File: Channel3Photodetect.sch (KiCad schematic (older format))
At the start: 5 parts

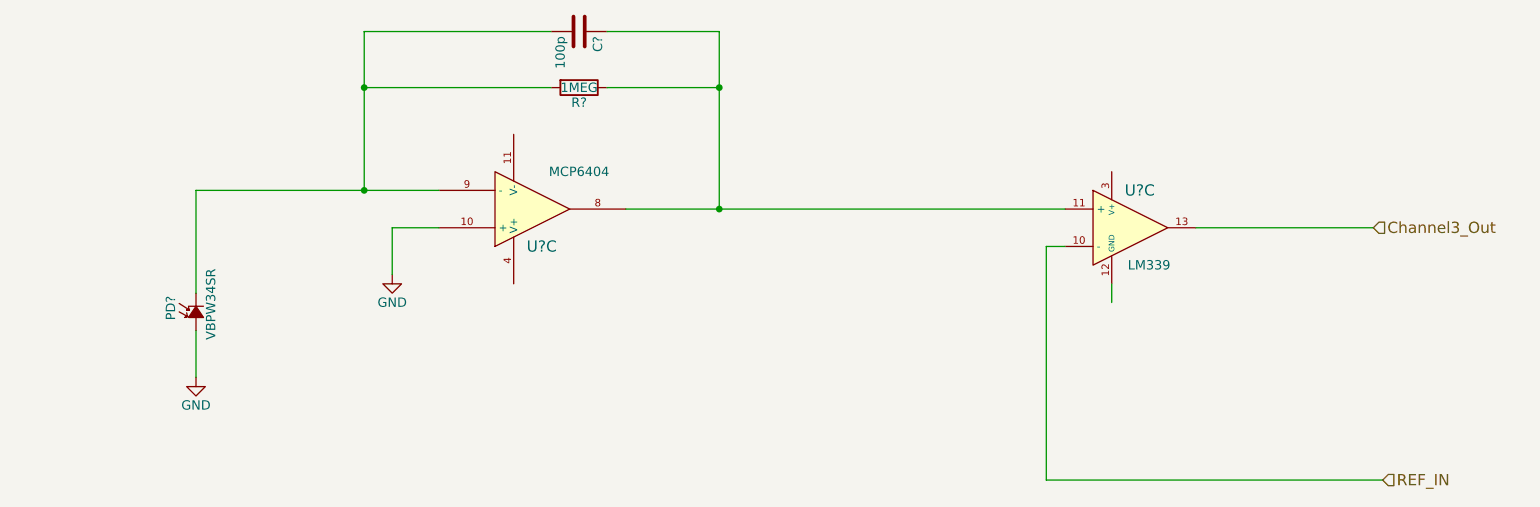
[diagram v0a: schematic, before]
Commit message: Added power regulator, VGND and test points
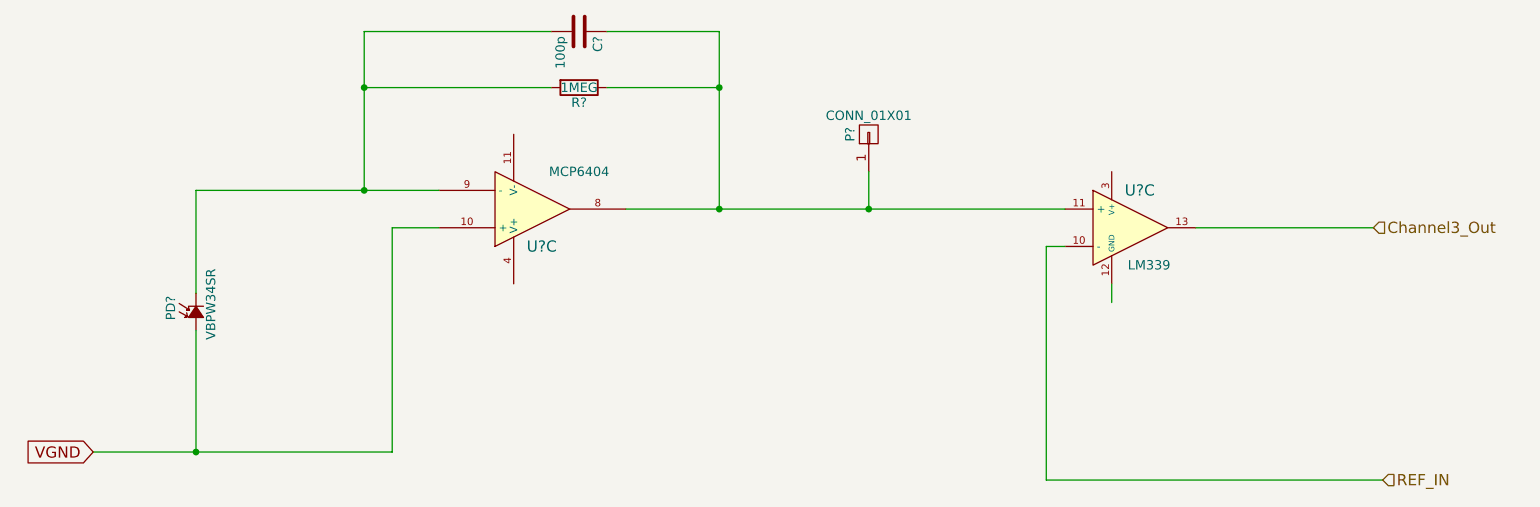
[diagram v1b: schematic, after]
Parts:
- added P?: CONN_01X01, symbol CONN_01X01
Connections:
- net labels added: VGND
- net labels removed: GND
- wire segments 17 -> 19
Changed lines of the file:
@@
 LIBS:memory
 LIBS:xilinx
-LIBS:special
 LIBS:microcontrollers
 LIBS:dsp
@@
 	4550 2350 5150 2350
 Connection ~ 5150 2650
-$Comp
-L GND #PWR?
-U 1 1 5552F9D9
-P 3400 3650
-F 0 "#PWR?" H 3400 3400 50  0001 C CNN
-F 1 "GND" H 3400 3500 50  0000 C CNN
-F 2 "" H 3400 3650 60  0000 C CNN
-F 3 "" H 3400 3650 60  0000 C CNN
-	1    3400 3650
-	1    0    0    -1
-$EndComp
 Wire Wire Line
 	3650 3400 3400 3400
 Wire Wire Line
-	3400 3400 3400 3650
-$Comp
-L GND #PWR?
-U 1 1 5552F9F4
-P 2350 4200
-F 0 "#PWR?" H 2350 3950 50  0001 C CNN
-F 1 "GND" H 2350 4050 50  0000 C CNN
-F 2 "" H 2350 4200 60  0000 C CNN
-F 3 "" H 2350 4200 60  0000 C CNN
-	1    2350 4200
-	1    0    0    -1
-$EndComp
+	3400 3400 3400 4600
 Wire Wire Line
-	2350 3950 2350 4200
+	2350 3950 2350 4600
 $Comp
 L LM339 U?
@@
 Wire Wire Line
 	6900 4750 6900 3500
+Wire Wire Line
+	3400 4600 1800 4600
+Text GLabel 1800 4600 0    60   Input ~ 0
+VGND
+Connection ~ 2350 4600
+$Comp
+L CONN_01X01 P?
+U 1 1 555630BF
+P 5950 2900
+F 0 "P?" H 5950 3000 50  0000 C CNN
+F 1 "CONN_01X01" V 6050 2900 50  0000 C CNN
+F 2 "" H 5950 2900 60  0000 C CNN
+F 3 "" H 5950 2900 60  0000 C CNN
+	1    5950 2900
+	0    -1   -1   0
+$EndComp
+Wire Wire Line
+	5950 3100 5950 3300
+Connection ~ 5950 3300
 $EndSCHEMATC

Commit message: Added libraries and imported components into the layout
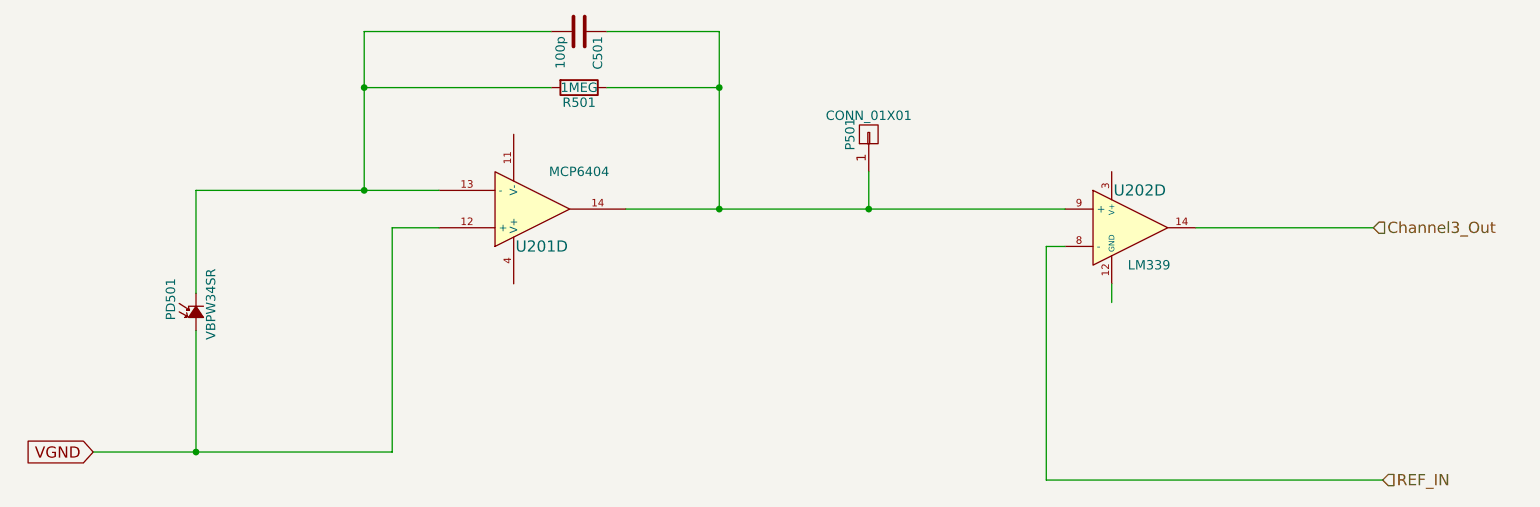
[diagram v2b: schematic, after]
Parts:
- gave numbers to parts that had none: 6
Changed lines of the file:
@@
 $EndDescr
 $Comp
-L R R?
+L R R501
 U 1 1 5552F9A4
 P 4400 2650
-F 0 "R?" V 4480 2650 50  0000 C CNN
+F 0 "R501" V 4480 2650 50  0000 C CNN
 F 1 "1MEG" V 4400 2650 50  0000 C CNN
 F 2 "" V 4330 2650 30  0000 C CNN
@@
 $EndComp
 $Comp
-L C C?
+L C C501
 U 1 1 5552F9AB
 P 4400 2350
-F 0 "C?" H 4425 2450 50  0000 L CNN
+F 0 "C501" H 4425 2450 50  0000 L CNN
 F 1 "100p" H 4425 2250 50  0000 L CNN
 F 2 "" H 4438 2200 30  0000 C CNN
@@
 $EndComp
 $Comp
-L MCP6404-E/SL U?
-U 3 1 5552F9B4
+L MCP6404-E/SL U201
+U 4 1 5552F9B4
 P 4150 3300
-F 0 "U?" H 4200 3500 60  0000 C CNN
+F 0 "U201" H 4200 3500 60  0000 C CNN
 F 1 "MCP6404" H 4400 3100 50  0000 C CNN
 F 2 "" H 4150 3300 60  0000 C CNN
@@
 F 4 "MCP6404-E/SL" H 4150 3300 60  0001 C CNN "MPN"
 F 5 "http://parts.io/detail/3584122/MCP6404-E%2FSL" H 4150 3300 60  0001 C CNN "Link"
-	3    4150 3300
+	4    4150 3300
 	1    0    0    1
 $EndComp
 $Comp
-L Photodiode PD?
+L Photodiode PD501
 U 1 1 5552F9BD
 P 2350 3850
-F 0 "PD?" H 2305 3985 50  0000 L CNN
+F 0 "PD501" H 2305 3985 50  0000 L CNN
 F 1 "VBPW34SR" H 2200 3770 50  0000 L CNN
 F 2 "" V 2350 3850 60  0000 C CNN
@@
 	2350 3950 2350 4600
 $Comp
-L LM339 U?
-U 3 1 5552F9FD
+L LM339 U202
+U 4 1 5552F9FD
 P 7350 3400
-F 0 "U?" H 7400 3600 60  0000 C CNN
+F 0 "U202" H 7400 3600 60  0000 C CNN
 F 1 "LM339" H 7450 3200 50  0000 C CNN
 F 2 "" H 7350 3400 60  0000 C CNN
@@
 F 4 "LM339DE4" H 7350 3400 60  0001 C CNN "MPN"
 F 5 "http://parts.io/detail/916254/LM339DE4" H 7350 3400 60  0001 C CNN "Link"
-	3    7350 3400
+	4    7350 3400
 	1    0    0    -1
 $EndComp
@@
 Connection ~ 2350 4600
 $Comp
-L CONN_01X01 P?
+L CONN_01X01 P501
 U 1 1 555630BF
 P 5950 2900
-F 0 "P?" H 5950 3000 50  0000 C CNN
+F 0 "P501" H 5950 3000 50  0000 C CNN
 F 1 "CONN_01X01" V 6050 2900 50  0000 C CNN
 F 2 "" H 5950 2900 60  0000 C CNN

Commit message: Added photodiode component to new local footprint library
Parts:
- C501: footprint (none) -> Capacitors_SMD:C_0805_HandSoldering
- P501: footprint (none) -> Pin_Headers:Pin_Header_Straight_1x01
- PD501: footprint (none) -> DasBlinkinput:VPW34SR
- R501: footprint (none) -> Resistors_SMD:R_1206_HandSoldering
- U201, U202: footprint (none) -> Housings_SOIC:SOIC-14_3.9x8.7mm_Pitch1.27mm
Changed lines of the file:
@@
 F 0 "R501" V 4480 2650 50  0000 C CNN
 F 1 "1MEG" V 4400 2650 50  0000 C CNN
-F 2 "" V 4330 2650 30  0000 C CNN
+F 2 "Resistors_SMD:R_1206_HandSoldering" V 4330 2650 30  0001 C CNN
 F 3 "" H 4400 2650 30  0000 C CNN
 F 4 "RC1206FR-071ML" V 4400 2650 60  0001 C CNN "MPN"
@@
 F 0 "C501" H 4425 2450 50  0000 L CNN
 F 1 "100p" H 4425 2250 50  0000 L CNN
-F 2 "" H 4438 2200 30  0000 C CNN
+F 2 "Capacitors_SMD:C_0805_HandSoldering" H 4438 2200 30  0001 C CNN
 F 3 "" H 4400 2350 60  0000 C CNN
 	1    4400 2350
@@
 F 0 "U201" H 4200 3500 60  0000 C CNN
 F 1 "MCP6404" H 4400 3100 50  0000 C CNN
-F 2 "" H 4150 3300 60  0000 C CNN
+F 2 "Housings_SOIC:SOIC-14_3.9x8.7mm_Pitch1.27mm" H 4150 3300 60  0001 C CNN
 F 3 "" H 4150 3300 60  0000 C CNN
 F 4 "MCP6404-E/SL" H 4150 3300 60  0001 C CNN "MPN"
@@
 F 0 "PD501" H 2305 3985 50  0000 L CNN
 F 1 "VBPW34SR" H 2200 3770 50  0000 L CNN
-F 2 "" V 2350 3850 60  0000 C CNN
+F 2 "DasBlinkinput:VPW34SR" V 2350 3850 60  0001 C CNN
 F 3 "" V 2350 3850 60  0000 C CNN
 F 4 "VBPW34SR" H 2350 3850 60  0001 C CNN "MPN"
@@
 F 0 "U202" H 7400 3600 60  0000 C CNN
 F 1 "LM339" H 7450 3200 50  0000 C CNN
-F 2 "" H 7350 3400 60  0000 C CNN
+F 2 "Housings_SOIC:SOIC-14_3.9x8.7mm_Pitch1.27mm" H 7350 3400 60  0001 C CNN
 F 3 "" H 7350 3400 60  0000 C CNN
 F 4 "LM339DE4" H 7350 3400 60  0001 C CNN "MPN"
@@
 F 0 "P501" H 5950 3000 50  0000 C CNN
 F 1 "CONN_01X01" V 6050 2900 50  0000 C CNN
-F 2 "" H 5950 2900 60  0000 C CNN
+F 2 "Pin_Headers:Pin_Header_Straight_1x01" H 5950 2900 60  0001 C CNN
 F 3 "" H 5950 2900 60  0000 C CNN
 	1    5950 2900

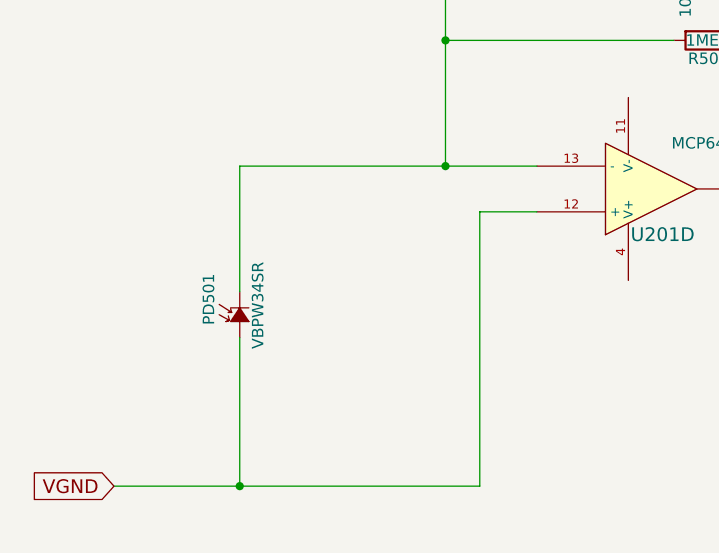
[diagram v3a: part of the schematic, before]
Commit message: Added secondary footprint for photodiode
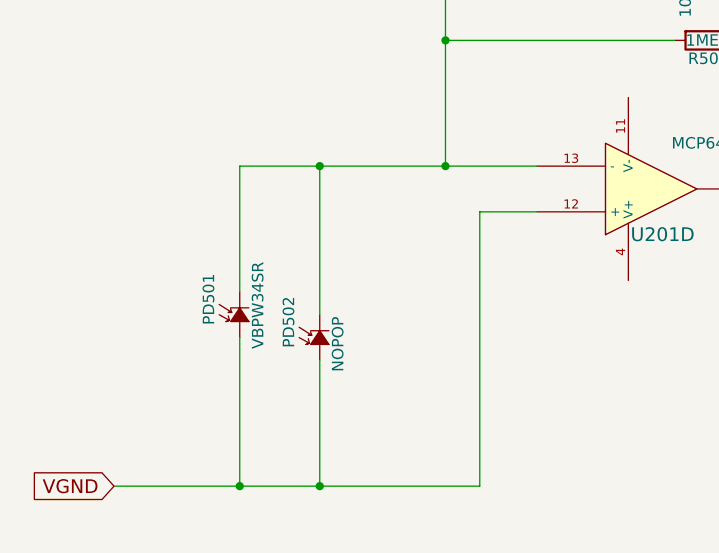
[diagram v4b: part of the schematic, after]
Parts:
- added PD502: NOPOP, Capacitors_SMD:C_0805_HandSoldering, symbol Photodiode
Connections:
- wire segments 19 -> 21
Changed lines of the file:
@@
 	5950 3100 5950 3300
 Connection ~ 5950 3300
+$Comp
+L Photodiode PD502
+U 1 1 555A3DD2
+P 2700 3950
+F 0 "PD502" H 2655 4085 50  0000 L CNN
+F 1 "NOPOP" H 2550 3870 50  0000 L CNN
+F 2 "Capacitors_SMD:C_0805_HandSoldering" V 2700 3950 60  0001 C CNN
+F 3 "" V 2700 3950 60  0000 C CNN
+F 4 "TEMD6200FX01" H 2700 3950 60  0001 C CNN "MPN"
+F 5 "http://parts.io/detail/2942502/TEMD6200FX01" H 2700 3950 60  0001 C CNN "Link"
+	1    2700 3950
+	0    -1   -1   0
+$EndComp
+Wire Wire Line
+	2700 3200 2700 3850
+Wire Wire Line
+	2700 4050 2700 4600
+Connection ~ 2700 3200
+Connection ~ 2700 4600
 $EndSCHEMATC

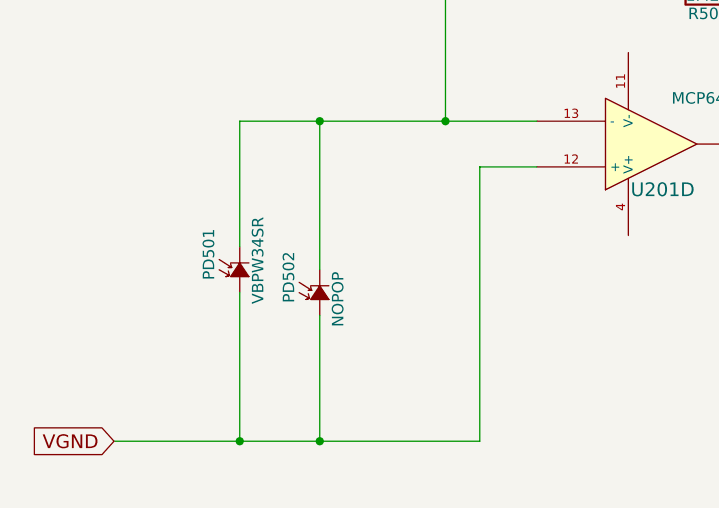
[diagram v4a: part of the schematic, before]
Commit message: Removing extra set of photodiodes and changing the original photodiode footprint
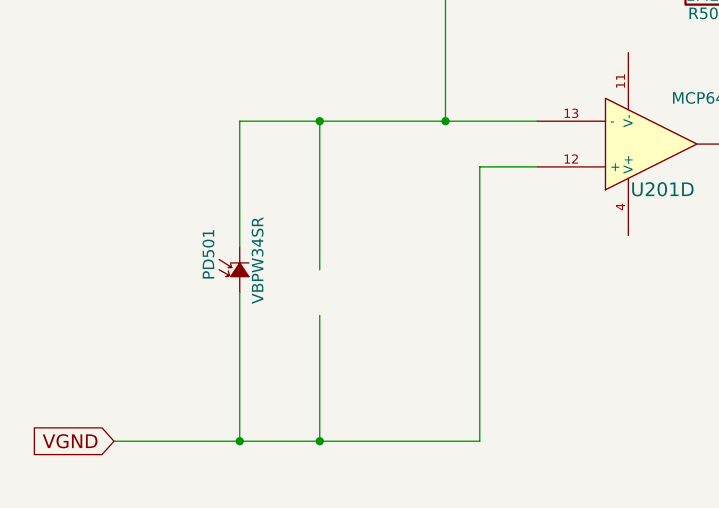
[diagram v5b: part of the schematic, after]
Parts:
- removed PD502: NOPOP, Capacitors_SMD:C_0805_HandSoldering, symbol Photodiode
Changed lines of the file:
@@
 	5950 3100 5950 3300
 Connection ~ 5950 3300
-$Comp
-L Photodiode PD502
-U 1 1 555A3DD2
-P 2700 3950
-F 0 "PD502" H 2655 4085 50  0000 L CNN
-F 1 "NOPOP" H 2550 3870 50  0000 L CNN
-F 2 "Capacitors_SMD:C_0805_HandSoldering" V 2700 3950 60  0001 C CNN
-F 3 "" V 2700 3950 60  0000 C CNN
-F 4 "TEMD6200FX01" H 2700 3950 60  0001 C CNN "MPN"
-F 5 "http://parts.io/detail/2942502/TEMD6200FX01" H 2700 3950 60  0001 C CNN "Link"
-	1    2700 3950
-	0    -1   -1   0
-$EndComp
 Wire Wire Line
 	2700 3200 2700 3850

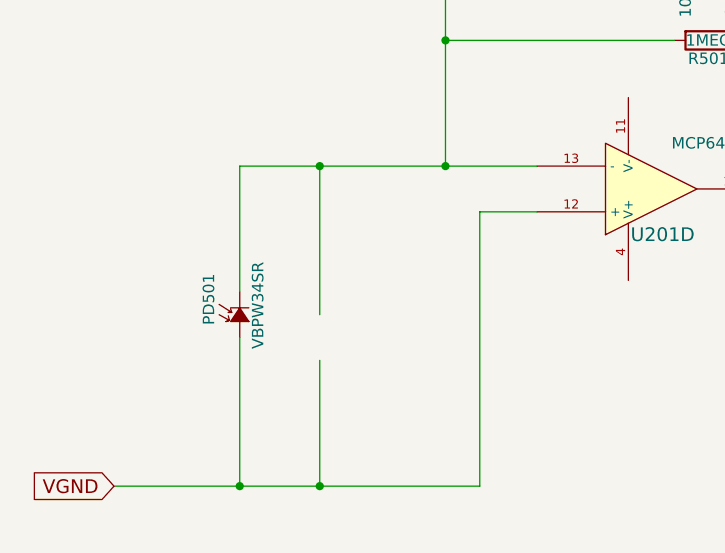
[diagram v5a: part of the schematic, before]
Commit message: Schematic and layout cleanup after photodiode removal
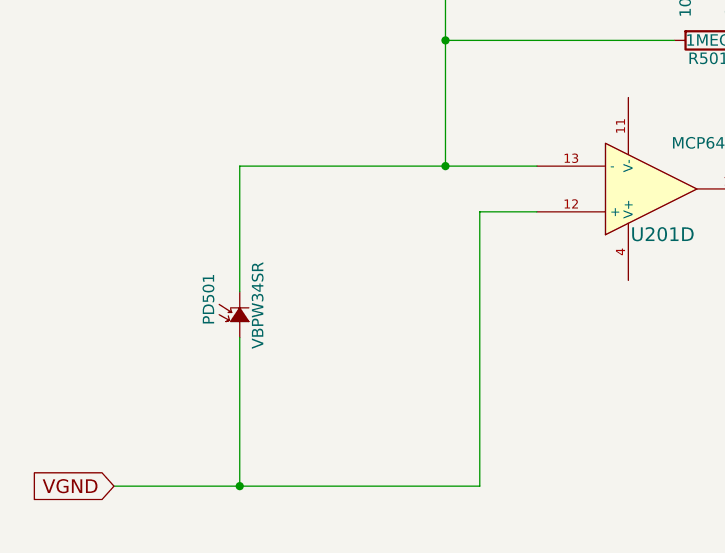
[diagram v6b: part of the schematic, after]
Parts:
- PD501: footprint DasBlinkinput:VPW34SR -> DasBlinkinput:VPW34SR*
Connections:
- wire segments 21 -> 19
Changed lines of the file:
@@
 F 0 "PD501" H 2305 3985 50  0000 L CNN
 F 1 "VBPW34SR" H 2200 3770 50  0000 L CNN
-F 2 "DasBlinkinput:VPW34SR" V 2350 3850 60  0001 C CNN
+F 2 "DasBlinkinput:VPW34SR*" V 2350 3850 60  0001 C CNN
 F 3 "" V 2350 3850 60  0000 C CNN
 F 4 "VBPW34SR" H 2350 3850 60  0001 C CNN "MPN"
@@
 	5950 3100 5950 3300
 Connection ~ 5950 3300
-Wire Wire Line
-	2700 3200 2700 3850
-Wire Wire Line
-	2700 4050 2700 4600
-Connection ~ 2700 3200
-Connection ~ 2700 4600
 $EndSCHEMATC

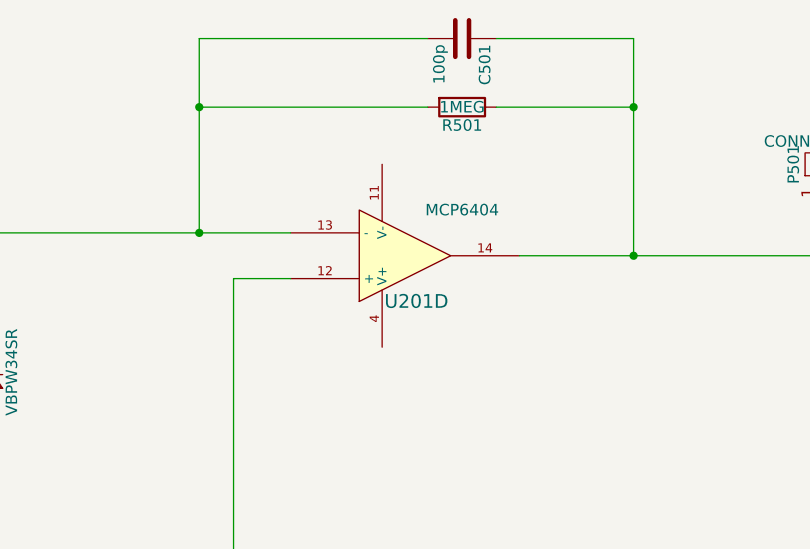
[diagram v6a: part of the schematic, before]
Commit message: Routed all passives related to U201 and the photodiodes
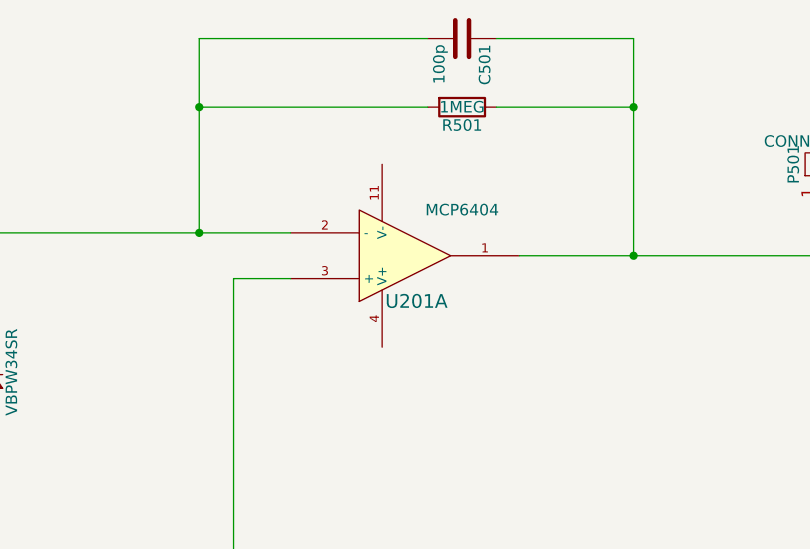
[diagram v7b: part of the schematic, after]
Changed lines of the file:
@@
 $Comp
 L MCP6404-E/SL U201
-U 4 1 5552F9B4
+U 1 1 5552F9B4
 P 4150 3300
 F 0 "U201" H 4200 3500 60  0000 C CNN
@@
 F 4 "MCP6404-E/SL" H 4150 3300 60  0001 C CNN "MPN"
 F 5 "http://parts.io/detail/3584122/MCP6404-E%2FSL" H 4150 3300 60  0001 C CNN "Link"
-	4    4150 3300
+	1    4150 3300
 	1    0    0    1
 $EndComp

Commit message: Routed remainder of lines and added test points with lables
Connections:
- net labels added: PD5
- net labels removed: Channel3_Out
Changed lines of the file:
@@
 $Comp
 L LM339 U202
-U 4 1 5552F9FD
+U 1 1 5552F9FD
 P 7350 3400
 F 0 "U202" H 7400 3600 60  0000 C CNN
@@
 F 4 "LM339DE4" H 7350 3400 60  0001 C CNN "MPN"
 F 5 "http://parts.io/detail/916254/LM339DE4" H 7350 3400 60  0001 C CNN "Link"
-	4    7350 3400
+	1    7350 3400
 	1    0    0    -1
 $EndComp
@@
 	7250 3700 7250 3800
 Text HLabel 8650 3400 2    60   Input ~ 0
-Channel3_Out
+PD5
 Text HLabel 8700 4750 2    60   Input ~ 0
 REF_IN
